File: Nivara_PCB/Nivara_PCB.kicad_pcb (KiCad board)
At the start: 2 copper layers, 102.2 x 83 mm, 67 parts, among them J1 NPN_IN, J10 Analog_Out, J11 RELAY, J2 PNP_IN, J3 D_IN, J4 Analaog_In, J5 RUN/STOP, J6 FUENTE, J7 NPN_OUT, J8 PNP_OUT, J9 RS485, Q1 IRLML6344, Q2 IRLML6344, Q3 IRLML6402, Q4 IRLML6402, U1 ESP32-S3-WROOM-1, U2 AP63203WU, U3 AP63205WU, U4 2920L185DR, U5 CUHZ30V,H3F, U7 CUHZ30V,H3F

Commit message: Cambios en la power supply.
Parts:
- removed U3: AP63205WU, Package_TO_SOT_SMD:TSOT-23-6
- added C11: 100pF, PCM_Capacitor_SMD_AKL:C_0805_2012Metric, F.Cu at (31.4, 164.5)
- added C12: 22uF, PCM_Capacitor_SMD_AKL:C_0603_1608Metric, F.Cu at (41.8, 163.1)
- added C13: 10uF, PCM_Capacitor_SMD_AKL:C_1206_3216Metric, F.Cu at (47.1, 169.8)
- added D2: SMBJ5.0A, PCM_Diode_SMD_AKL:D_SMB, F.Cu at (62.4, 75.6)
- added D3: SMBJ12CA, PCM_Diode_SMD_AKL:D_SMB_TVS, F.Cu at (53.9, 75.2)
- added D4: SMBJ33A, PCM_Diode_SMD_AKL:D_SMB, F.Cu at (71.7, 29.3)
- added D5: SMBJ33A, PCM_Diode_SMD_AKL:D_SMB, F.Cu at (29.9, 91.1)
- added D6: SMBJ33A, PCM_Diode_SMD_AKL:D_SMB, F.Cu at (71.7, 35.8)
- added D7: SMBJ33A, PCM_Diode_SMD_AKL:D_SMB, F.Cu at (43.4, 57.8)
- added D8: SMBJ33A, PCM_Diode_SMD_AKL:D_SMB, F.Cu at (43.4, 64.3)
- added J12: Analaog_In, TerminalBlock:TerminalBlock_bornier-4_P5.08mm, F.Cu at (28.9, 83.3)
- added JP1: SolderJumper_2_Open, Jumper:SolderJumper-2_P1.3mm_Open_Pad1.0x1.5mm, F.Cu at (41.8, 166.2)
- added JP2: SolderJumper_2_Open, Jumper:SolderJumper-2_P1.3mm_Open_Pad1.0x1.5mm, F.Cu at (41.8, 169.8)
- added L3: CXP0420-6R8M-AG(6.8UH), Fuse_Holder:IND-SMD_L4.4-W4.2_CXP0420, F.Cu at (36.8, 161.8)
- added Q10: SS8550, Package_TO_SOT_SMD:SOT-23, F.Cu at (69.9, 46.1)
- added Q14: ZXMS6004DGTA, Fuse_Holder:SOT-223-3_L6.5-W3.4-P2.30-LS7.0-BR, F.Cu at (47.2, 37.8)
- added Q15: ZXMS6004DGTA, Fuse_Holder:SOT-223-3_L6.5-W3.4-P2.30-LS7.0-BR, F.Cu at (62.7, 30.0)
- added Q16: ZXMS6004DGTA, Fuse_Holder:SOT-223-3_L6.5-W3.4-P2.30-LS7.0-BR, F.Cu at (62.7, 37.8)
- added Q17: SS8050, Package_TO_SOT_SMD:SOT-23, F.Cu at (41.6, 74.6)
- added Q18: ZXMS6004DGTA, Fuse_Holder:SOT-223-3_L6.5-W3.4-P2.30-LS7.0-BR, F.Cu at (34.4, 66.3)
- added Q6: SS8050, Package_TO_SOT_SMD:SOT-23, F.Cu at (41.6, 70.0)
- added Q7: ZXMS6004DGTA, Fuse_Holder:SOT-223-3_L6.5-W3.4-P2.30-LS7.0-BR, F.Cu at (34.4, 58.5)
- added Q8: ZXMS6004DGTA, Fuse_Holder:SOT-223-3_L6.5-W3.4-P2.30-LS7.0-BR, F.Cu at (47.2, 30.0)
- added Q9: SS8550, Package_TO_SOT_SMD:SOT-23, F.Cu at (69.9, 41.5)
- added R20: 2K2, PCM_Resistor_SMD_AKL:R_0603_1608Metric, F.Cu at (27.7, 55.9)
- added R21: 1k, PCM_Resistor_SMD_AKL:R_0603_1608Metric, F.Cu at (27.7, 58.6)
- added R22: 2k, PCM_Resistor_SMD_AKL:R_0603_1608Metric, F.Cu at (27.7, 61.4)
- added R23: 22k, PCM_Resistor_SMD_AKL:R_0603_1608Metric, F.Cu at (27.7, 64.1)
- added R24: 2K2, PCM_Resistor_SMD_AKL:R_0603_1608Metric, F.Cu at (27.7, 66.8)
- added R25: 2K2, PCM_Resistor_SMD_AKL:R_0603_1608Metric, F.Cu at (56.0, 27.4)
- added R26: 1k, PCM_Resistor_SMD_AKL:R_0603_1608Metric, F.Cu at (56.0, 30.1)
- added R27: 2k, PCM_Resistor_SMD_AKL:R_0603_1608Metric, F.Cu at (56.0, 32.9)
- added R28: 22k, PCM_Resistor_SMD_AKL:R_0603_1608Metric, F.Cu at (56.0, 35.6)
- added R29: 2K2, PCM_Resistor_SMD_AKL:R_0603_1608Metric, F.Cu at (56.0, 38.3)
- added R30: R_0603, PCM_Resistor_SMD_AKL:R_0603_1608Metric, F.Cu at (48.4, 102.4)
- added R31: 196k, PCM_Resistor_SMD_AKL:R_0603_1608Metric, F.Cu at (46.0, 154.9)
- added R32: 62k, PCM_Resistor_SMD_AKL:R_0603_1608Metric, F.Cu at (46.0, 157.7)
- added R33: 157k, PCM_Resistor_SMD_AKL:R_0603_1608Metric, F.Cu at (46.0, 160.4)
- added R34: 30k, PCM_Resistor_SMD_AKL:R_0603_1608Metric, F.Cu at (46.0, 163.1)
- added R40: 1k, PCM_Resistor_SMD_AKL:R_0603_1608Metric, F.Cu at (44.6, 43.0)
- added R41: 1k, PCM_Resistor_SMD_AKL:R_0603_1608Metric, F.Cu at (56.0, 41.0)
- added R42: 22k, PCM_Resistor_SMD_AKL:R_0603_1608Metric, F.Cu at (44.6, 45.8)
- added R43: 1k, PCM_Resistor_SMD_AKL:R_0603_1608Metric, F.Cu at (44.6, 48.5)
- added R44: 22k, PCM_Resistor_SMD_AKL:R_0603_1608Metric, F.Cu at (44.6, 51.2)
- added R45: 2k, PCM_Resistor_SMD_AKL:R_0603_1608Metric, F.Cu at (56.0, 43.7)
- added R46: 22k, PCM_Resistor_SMD_AKL:R_0603_1608Metric, F.Cu at (56.0, 46.5)
- added R47: 1k, PCM_Resistor_SMD_AKL:R_0603_1608Metric, F.Cu at (27.7, 69.5)
- added R48: 2k, PCM_Resistor_SMD_AKL:R_0603_1608Metric, F.Cu at (27.7, 72.2)
- added R49: 22k, PCM_Resistor_SMD_AKL:R_0603_1608Metric, F.Cu at (27.7, 75.0)
- added RLY1: JY4101F-S-DC5V-C, Fuse_Holder:RELAY-TH_HK4101F-XX-XX_XX, F.Cu at (34.1, 31.9)
- added RLY2: JY4101F-S-DC5V-C, Fuse_Holder:RELAY-TH_HK4101F-XX-XX_XX, F.Cu at (34.1, 43.8)
- added TP5: +5Vout, TestPoint:TestPoint_Pad_1.0x1.0mm, F.Cu at (36.6, 149.0)
- added TP6: +5V, TestPoint:TestPoint_Pad_1.0x1.0mm, F.Cu at (36.6, 152.1)
- added TP7: +3.3Vout, TestPoint:TestPoint_Pad_1.0x1.0mm, F.Cu at (39.7, 149.0)
- added TP8: FB, TestPoint:TestPoint_Pad_1.0x1.0mm, F.Cu at (39.7, 152.1)
- added U5: XTR115UA, Fuse_Holder:SOIC-8_L4.9-W3.9-P1.27-LS6.0-BL, F.Cu at (43.3, 105.3)
- added U6: RSM3485ECHT_C2992406, Fuse_Holder:COMM-TH_8P-L19.5-W16.5-P2.54-BL, F.Cu at (60.1, 63.5)
- C10: value 1uF -> 10uF
- C3: value 10uF -> 22uF; footprint PCM_Capacitor_SMD_AKL:C_1206_3216Metric -> PCM_Capacitor_SMD_AKL:C_0603_1608Metric
- C7: value 22uF -> 100pF
- C8, C9: footprint PCM_Capacitor_SMD_AKL:C_0805_2012Metric -> PCM_Capacitor_SMD_AKL:C_0603_1608Metric
- L1: value 4u7H -> CXP0420-6R8M-AG(6.8UH); footprint Inductor_SMD:L_APV_ANR6028 -> Fuse_Holder:IND-SMD_L4.4-W4.2_CXP0420
- L2: value 4u7H -> 10uH
- R12, R16: value 1k -> 500
- R2, R6: value 7k -> 42k
- TP4: value +5V -> FB
- U2: value AP63203WU -> AP63200WU
- U7: value CUHZ30V,H3F -> AP63200WU; footprint Fuse_Holder:SOD-323HE_L2.0-W1.4-LS2.5-RD -> Package_TO_SOT_SMD:TSOT-23-6
- moved C7 127.1 mm to (31.4, 161.4), turned to 0 degrees
- moved C5 125.4 mm to (31.4, 158.3), turned to 0 degrees
- moved TP4 120.4 mm to (33.6, 152.1), turned to 0 degrees
- moved TP3 118.9 mm to (33.6, 149.0), turned to 0 degrees
- moved C9 118.3 mm to (41.8, 160.4), turned to 0 degrees
- moved C8 116.2 mm to (41.8, 157.7)
- moved L1 116.2 mm to (36.8, 156.3), turned to 0 degrees
- moved TP2 115.2 mm to (30.5, 152.1), turned to 0 degrees
- moved C4 114.1 mm to (31.4, 155.2), turned to 0 degrees
- moved C2 113.4 mm to (47.1, 166.2), turned to 0 degrees
- moved TP1 111.4 mm to (30.5, 149.0), turned to 0 degrees
- moved C3 110.4 mm to (41.8, 155.0), turned to 0 degrees
- moved U2 105.4 mm to (50.7, 156.0), turned to 0 degrees
- moved U7 96.6 mm to (50.7, 160.6)
- moved L2 95.2 mm to (66.6, 140.7), turned to 0 degrees
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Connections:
- C3 pad 1: VCC -> Net-(JP1-A)
- C4 pad 1: Net-(U2-BST) -> Net-(U7-BST)
- C4 pad 2: Net-(U2-SW) -> Net-(U7-SW)
- C5 pad 1: Net-(U3-BST) -> Net-(U2-BST)
- C5 pad 2: Net-(U3-SW) -> Net-(U2-SW)
- C7 pad 1: +5V -> Net-(U2-FB)
- C7 pad 2: GND -> Net-(JP2-A)
- C8 pad 1: +3.3V -> Net-(JP2-A)
- C9 pad 1: +5V -> Net-(JP2-A)
- D1 pad 2: Net-(D1-A2) -> Net-(D1-A1)
- J4 pad 1: /NIVARA_BOARD/A0_10_IN_1 -> /NIVARA_BOARD/A0_5_IN_1
- J4 pad 2: /NIVARA_BOARD/A0_32_IN_1 -> /NIVARA_BOARD/A0_10_IN_1
- L1 pad 2: +3.3V -> Net-(JP2-A)
- L2 pad 1: Net-(U3-SW) -> Net-(U2-SW)
- L2 pad 2: +5V -> +3.3V
- R19 pad 1: Net-(D1-A2) -> Net-(D1-A1)
- TP3 pad 1: +3.3V -> Net-(JP1-A)
- TP4 pad 1: +5V -> Net-(U7-FB)
- U2 pad 1: +3.3V -> Net-(U2-FB)
- U7 pad 1: +3.3V -> Net-(U7-FB)
- U7 pad 2: GND -> VCC
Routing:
- net +5V: track 81.3 -> 35.2 mm, vias 4 -> 3
- net +3.3V: track 67.1 -> 24.3 mm, vias 4 -> 3
- net VCC: track 27.6 -> 0.00 mm
- net Net-(U2-SW): track 11.2 -> 0.00 mm
- net Net-(J6-Pin_1): track 7.46 -> 0.00 mm
- net Net-(U3-SW): track 7.10 -> 0.00 mm
- net Net-(U2-BST): track 2.77 -> 0.00 mm
- net Net-(U3-BST): track 2.55 -> 0.00 mm
- net GND: vias 33 -> 17
- net (no net): vias 0 -> 1
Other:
- copper layers 2 -> 4

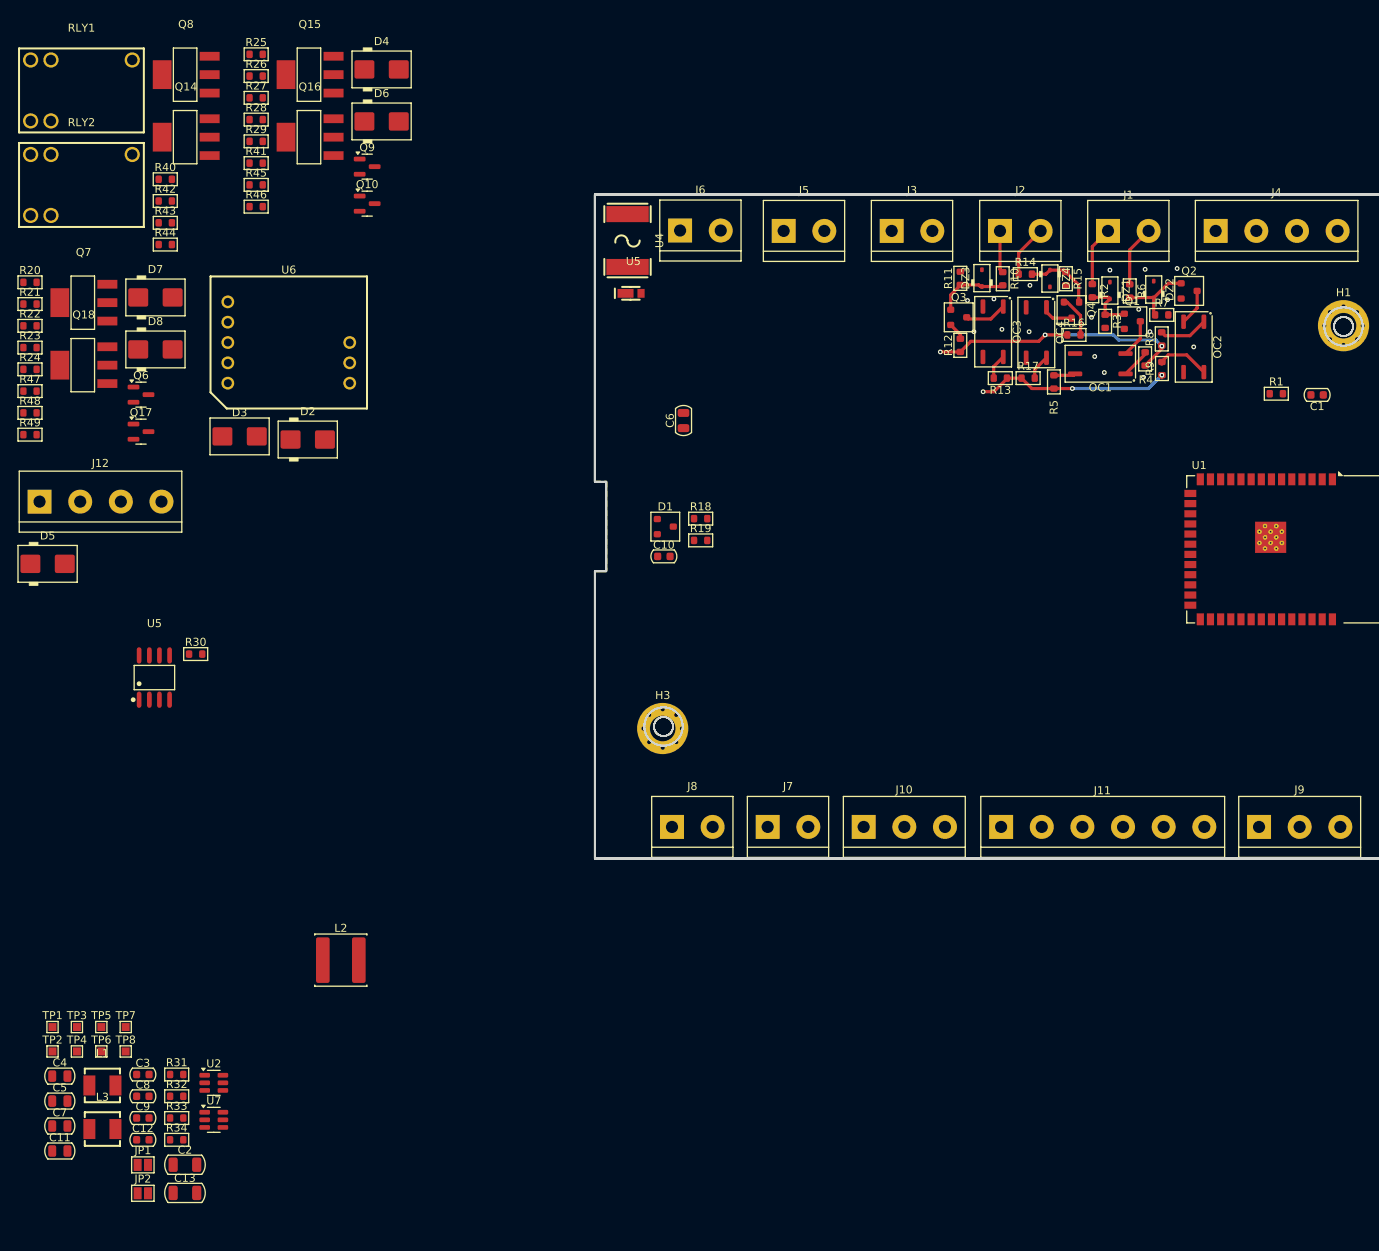
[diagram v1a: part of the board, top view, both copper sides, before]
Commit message: Cambios en las salidas analogicas, ya que el ESP32 S3 no tiene DAC
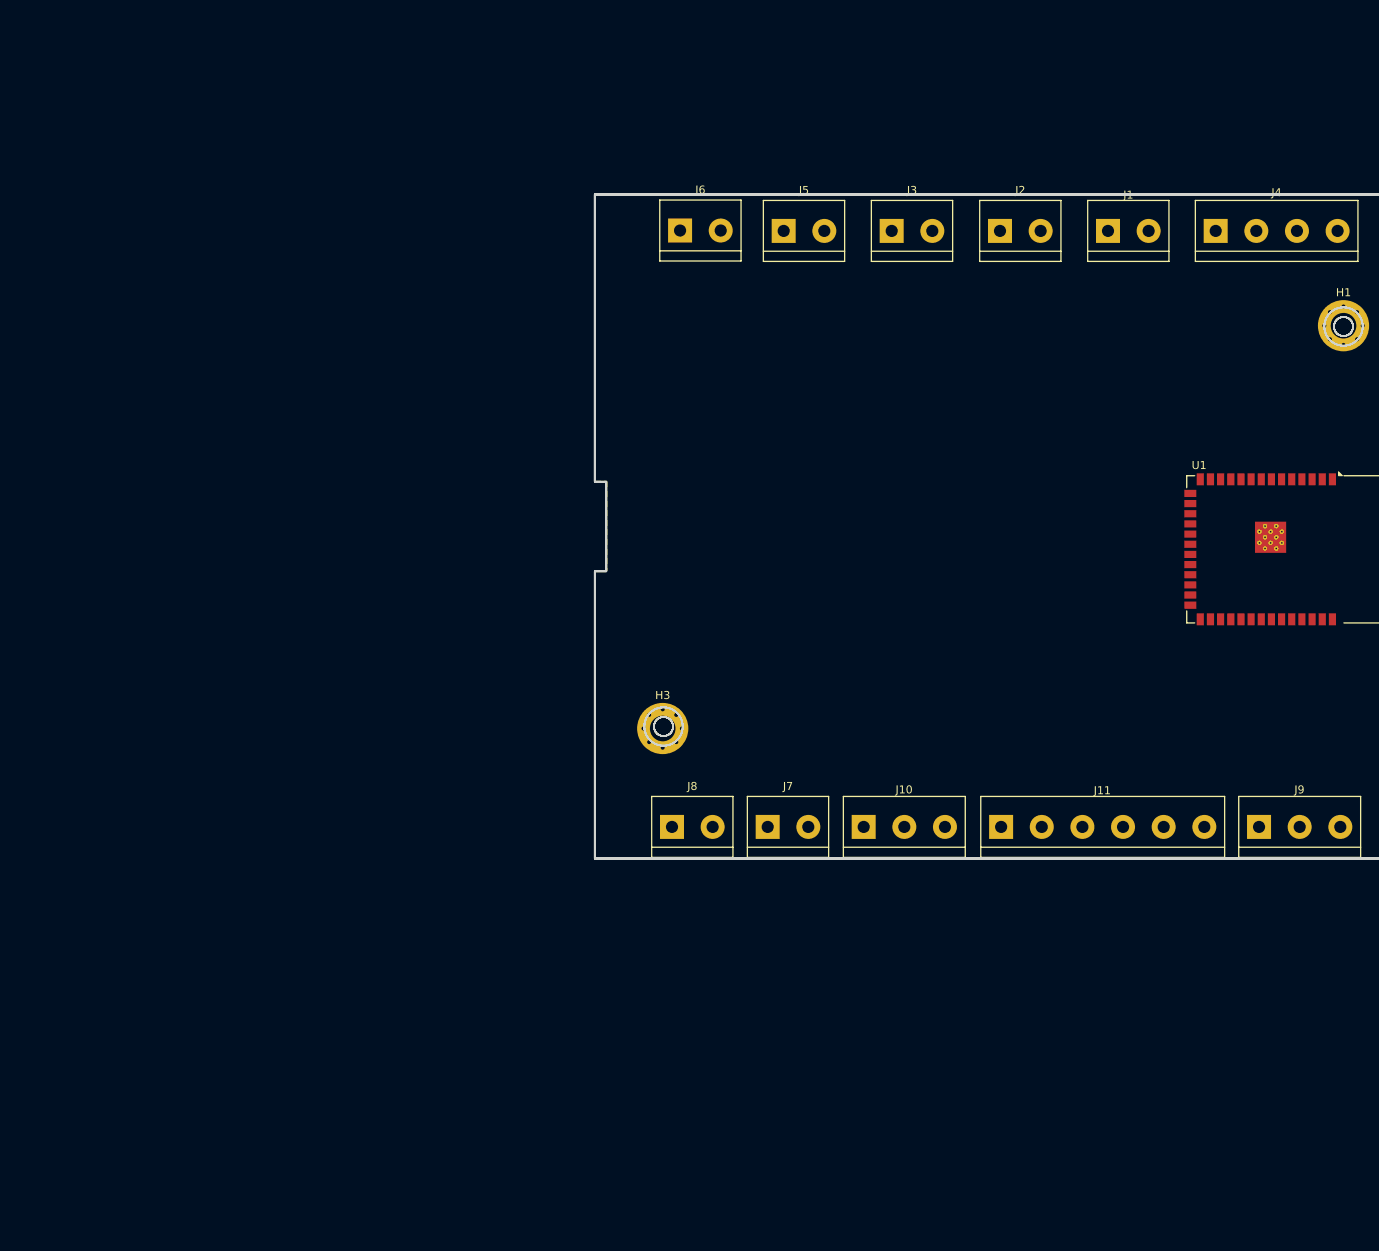
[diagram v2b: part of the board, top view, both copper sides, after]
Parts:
- removed C1: 1uF, PCM_Capacitor_SMD_AKL:C_0603_1608Metric
- removed C10: 10uF, PCM_Capacitor_SMD_AKL:C_0603_1608Metric
- removed C11, C7: 100pF, PCM_Capacitor_SMD_AKL:C_0805_2012Metric
- removed C12, C3, C8, C9: 22uF, PCM_Capacitor_SMD_AKL:C_0603_1608Metric
- removed C13, C2: 10uF, PCM_Capacitor_SMD_AKL:C_1206_3216Metric
- removed C4, C5: 100nF, PCM_Capacitor_SMD_AKL:C_0805_2012Metric
- removed C6: 22uF, PCM_Capacitor_SMD_AKL:C_0805_2012Metric
- removed D1: SM712, PCM_Package_TO_SOT_SMD_AKL:SOT-23
- removed D2: SMBJ5.0A, PCM_Diode_SMD_AKL:D_SMB
- removed D3: SMBJ12CA, PCM_Diode_SMD_AKL:D_SMB_TVS
- removed D4, D5, D6, D7, D8: SMBJ33A, PCM_Diode_SMD_AKL:D_SMB
- removed DZ1, DZ2, DZ3, DZ4: BZT52C10S, PCM_Diode_SMD_AKL:D_SOD-323
- removed J12: Analaog_In, TerminalBlock:TerminalBlock_bornier-4_P5.08mm
- removed JP1, JP2: SolderJumper_2_Open, Jumper:SolderJumper-2_P1.3mm_Open_Pad1.0x1.5mm
- removed L1, L3: CXP0420-6R8M-AG(6.8UH), Fuse_Holder:IND-SMD_L4.4-W4.2_CXP0420
- removed L2: 10uH, Inductor_SMD:L_APV_ANR6028
- removed OC1, OC2, OC3, OC4: LTV-356T, PCM_Package_SO_AKL:SO-4_4.4x3.9mm_P2.54mm
- removed Q1, Q2: IRLML6344, PCM_Package_TO_SOT_SMD_AKL:SOT-23
- removed Q10, Q9: SS8550, Package_TO_SOT_SMD:SOT-23
- removed Q14, Q15, Q16, Q18, Q7, Q8: ZXMS6004DGTA, Fuse_Holder:SOT-223-3_L6.5-W3.4-P2.30-LS7.0-BR
- removed Q17, Q6: SS8050, Package_TO_SOT_SMD:SOT-23
- removed Q3, Q4: IRLML6402, PCM_Package_TO_SOT_SMD_AKL:SOT-23
- removed R1, R18, R19, R30: R_0603, PCM_Resistor_SMD_AKL:R_0603_1608Metric
- removed R10, R14: 7k, PCM_Resistor_SMD_AKL:R_0603_1608Metric
- removed R11, R15, R23, R28, R3, R42, R44, R46, R49, R7: 22k, PCM_Resistor_SMD_AKL:R_0603_1608Metric
- removed R12, R16: 500, PCM_Resistor_SMD_AKL:R_0603_1608Metric
- removed R13, R17, R5, R9: 10k, PCM_Resistor_SMD_AKL:R_0603_1608Metric
- removed R2, R6: 42k, PCM_Resistor_SMD_AKL:R_0603_1608Metric
- removed R20, R24, R25, R29: 2K2, PCM_Resistor_SMD_AKL:R_0603_1608Metric
- removed R21, R26, R4, R40, R41, R43, R47, R8: 1k, PCM_Resistor_SMD_AKL:R_0603_1608Metric
- removed R22, R27, R45, R48: 2k, PCM_Resistor_SMD_AKL:R_0603_1608Metric
- removed R31: 196k, PCM_Resistor_SMD_AKL:R_0603_1608Metric
- removed R32: 62k, PCM_Resistor_SMD_AKL:R_0603_1608Metric
- removed R33: 157k, PCM_Resistor_SMD_AKL:R_0603_1608Metric
- removed R34: 30k, PCM_Resistor_SMD_AKL:R_0603_1608Metric
- removed RLY1, RLY2: JY4101F-S-DC5V-C, Fuse_Holder:RELAY-TH_HK4101F-XX-XX_XX
- removed TP1: +VCC, TestPoint:TestPoint_Pad_1.0x1.0mm
- removed TP2: GND, TestPoint:TestPoint_Pad_1.0x1.0mm
- removed TP3: +3.3V, TestPoint:TestPoint_Pad_1.0x1.0mm
- removed TP4, TP8: FB, TestPoint:TestPoint_Pad_1.0x1.0mm
- removed TP5: +5Vout, TestPoint:TestPoint_Pad_1.0x1.0mm
- removed TP6: +5V, TestPoint:TestPoint_Pad_1.0x1.0mm
- removed TP7: +3.3Vout, TestPoint:TestPoint_Pad_1.0x1.0mm
- removed U2, U7: AP63200WU, Package_TO_SOT_SMD:TSOT-23-6
- removed U4: 2920L185DR, Fuse_Holder:F2920
- removed U5: CUHZ30V,H3F, Fuse_Holder:SOD-323HE_L2.0-W1.4-LS2.5-RD
- removed U5: XTR115UA, Fuse_Holder:SOIC-8_L4.9-W3.9-P1.27-LS6.0-BL
- removed U6: RSM3485ECHT_C2992406, Fuse_Holder:COMM-TH_8P-L19.5-W16.5-P2.54-BL
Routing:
- net +5V: track 35.2 -> 0.00 mm, vias 3 -> 0
- net +3.3V: track 24.3 -> 0.00 mm, vias 3 -> 0
- net Net-(DZ2-K): track 9.40 -> 0.00 mm
- net Net-(DZ3-K): track 9.04 -> 0.00 mm
- net Net-(DZ4-K): track 8.99 -> 0.00 mm
- net /NIVARA_BOARD/NPN_IN_2: track 7.65 -> 0.00 mm
- net /NIVARA_BOARD/NPN_IN_1: track 7.46 -> 0.00 mm
- net Net-(DZ1-K): track 6.96 -> 0.00 mm
- net /NIVARA_BOARD/NPN_IN/ESP_NPN_IN_2: track 6.85 -> 0.00 mm
- net /NIVARA_BOARD/PNP_IN_2: track 6.53 -> 0.00 mm
- net Net-(OC2-Pad1): track 6.17 -> 0.00 mm
- net Net-(Q3-D): track 5.29 -> 0.00 mm
- net /NIVARA_BOARD/PNP_IN_1: track 5.29 -> 0.00 mm
- net Net-(Q4-S): track 5.19 -> 0.00 mm
- net Net-(Q1-D): track 4.80 -> 0.00 mm
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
